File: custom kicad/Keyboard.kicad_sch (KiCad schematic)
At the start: 1 part, among them U1 nRF52840

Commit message: started custom pcb
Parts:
- removed U1: nRF52840, Package_DFN_QFN:Nordic_AQFN-73-1EP_7x7mm_P0.5mm, symbol MCU_Nordic:nRF52840
- added D1, D10, D100, D101, D102, D11, D12, D13, D14, D15, D16, D17, D18, D19, D2, D20, D21, D22, D23, D24, D25, D26, D27, D28, D29, D3, D30, D32, D33, D34, D35, D36, D39, D4, D40, D41, D42, D43, D44, D45, D46, D47, D48, D49, D5, D50, D51, D52, D53, D54, D55, D56, D57, D58, D59, D6, D60, D61, D62, D63, D65, D66, D67, D68, D7, D70, D71, D72, D73, D75, D76, D77, D78, D79, D8, D81, D83, D84, D85, D87, D89, D9, D91, D92, D94, D95, D96, D98, D99: D_Small, symbol Device:D_Small
- added J1: Conn_02x20_Top_Bottom, symbol Connector_Generic:Conn_02x20_Top_Bottom
- added MX1, MX10, MX100, MX101, MX102, MX11, MX12, MX13, MX14, MX15, MX16, MX17, MX18, MX19, MX2, MX20, MX21, MX22, MX23, MX24, MX25, MX26, MX27, MX28, MX29, MX3, MX30, MX32, MX33, MX34, MX35, MX36, MX39, MX4, MX40, MX41, MX42, MX43, MX44, MX45, MX46, MX47, MX48, MX49, MX5, MX50, MX51, MX52, MX53, MX54, MX55, MX56, MX57, MX58, MX59, MX6, MX60, MX61, MX62, MX63, MX65, MX66, MX67, MX68, MX7, MX70, MX71, MX72, MX73, MX75, MX76, MX77, MX78, MX79, MX8, MX81, MX83, MX84, MX85, MX87, MX89, MX9, MX91, MX92, MX94, MX95, MX96, MX98, MX99: MX_SW_HS, PCM_marbastlib-mx:SW_MX_HS_CPG151101S11_1u, symbol marbastlib-mx:MX_SW_HS_CPG151101S11
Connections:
- new net: D67.2 (A), MX67.2
- new net: D48.2 (A), MX48.2
- new net: D81.2 (A), MX81.2
- new net: D41.2 (A), MX41.2
- new net: D77.2 (A), MX77.2
- new net: D42.2 (A), MX42.2
- new net: D53.2 (A), MX53.2
- new net: D91.2 (A), MX91.2
- new net: D56.2 (A), MX56.2
- new net: D33.2 (A), MX33.2
- new net: D30.2 (A), MX30.2
- new net: D40.2 (A), MX40.2
- new net: D36.2 (A), MX36.2
- new net: D50.2 (A), MX50.2
- new net: D26.2 (A), MX26.2
- new net: D49.2 (A), MX49.2
- new net: D19.2 (A), MX19.2
- new net: D92.2 (A), MX92.2
- new net: D73.2 (A), MX73.2
- new net: D8.2 (A), MX8.2
- new net: D79.2 (A), MX79.2
- new net: D22.2 (A), MX22.2
- new net: D6.2 (A), MX6.2
- new net: D78.2 (A), MX78.2
- new net: D39.2 (A), MX39.2
- new net: D58.2 (A), MX58.2
- new net: D96.2 (A), MX96.2
- new net: D13.2 (A), MX13.2
- new net: D68.2 (A), MX68.2
- new net: D14.2 (A), MX14.2
- new net: D34.2 (A), MX34.2
- new net: D83.2 (A), MX83.2
- new net: D102.2 (A), MX102.2
- new net: D44.2 (A), MX44.2
- new net: D65.2 (A), MX65.2
- new net: D11.2 (A), MX11.2
- new net: D54.2 (A), MX54.2
- new net: D87.2 (A), MX87.2
- new net: D101.2 (A), MX101.2
- new net: D57.2 (A), MX57.2
- new net: D20.2 (A), MX20.2
- new net: D59.2 (A), MX59.2
- new net: D12.2 (A), MX12.2
- new net: D24.2 (A), MX24.2
- new net: D47.2 (A), MX47.2
- new net: D18.2 (A), MX18.2
- new net: D55.2 (A), MX55.2
- new net: D1.2 (A), MX1.2
- new net: D94.2 (A), MX94.2
- new net: D100.2 (A), MX100.2
- new net: D29.2 (A), MX29.2
- new net: D72.2 (A), MX72.2
- new net: D66.2 (A), MX66.2
- new net: D95.2 (A), MX95.2
- new net: D46.2 (A), MX46.2
- new net: D17.2 (A), MX17.2
- new net: D25.2 (A), MX25.2
- new net: D99.2 (A), MX99.2
- new net: D71.2 (A), MX71.2
- new net: D62.2 (A), MX62.2
- new net: D3.2 (A), MX3.2
- new net: D76.2 (A), MX76.2
- new net: D85.2 (A), MX85.2
- new net: D2.2 (A), MX2.2
- new net: D32.2 (A), MX32.2
- new net: D10.2 (A), MX10.2
- new net: D27.2 (A), MX27.2
- new net: D5.2 (A), MX5.2
- new net: D61.2 (A), MX61.2
- new net: D84.2 (A), MX84.2
- new net: D21.2 (A), MX21.2
- new net: D70.2 (A), MX70.2
- new net: D23.2 (A), MX23.2
- new net: D52.2 (A), MX52.2
- new net: D7.2 (A), MX7.2
- new net: D15.2 (A), MX15.2
- new net: D28.2 (A), MX28.2
- new net: D51.2 (A), MX51.2
- new net: D4.2 (A), MX4.2
- new net: D63.2 (A), MX63.2
- new net: D9.2 (A), MX9.2
- new net: D45.2 (A), MX45.2
- new net: D98.2 (A), MX98.2
- new net: D60.2 (A), MX60.2
- new net: D43.2 (A), MX43.2
- new net: D89.2 (A), MX89.2
- new net: D75.2 (A), MX75.2
- new net: D16.2 (A), MX16.2
- new net: D35.2 (A), MX35.2
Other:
- removed sheet MCU

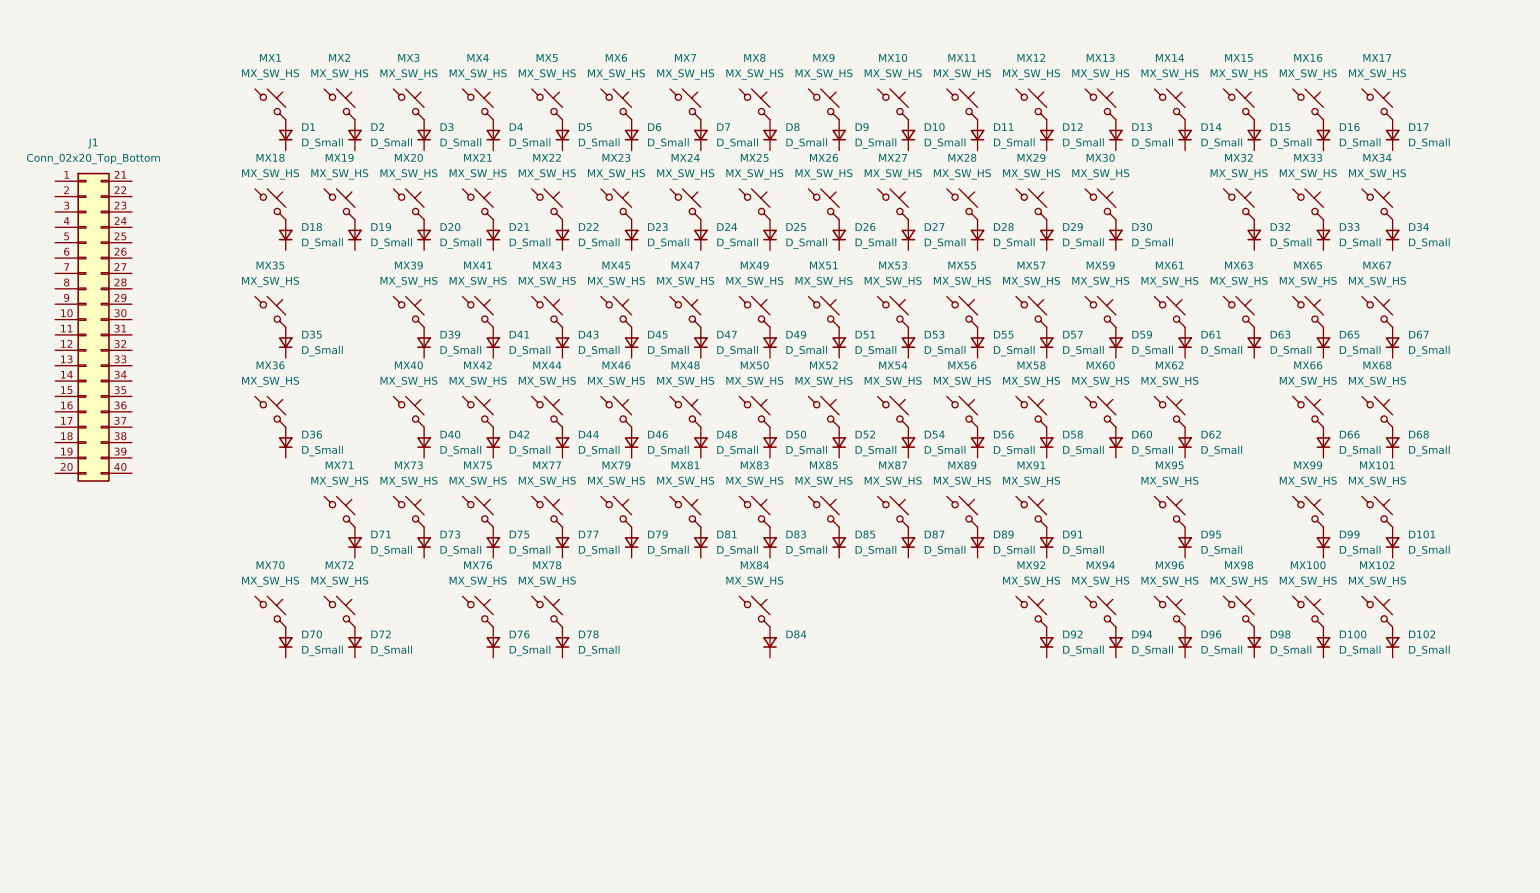
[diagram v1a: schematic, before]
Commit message: wired custom pcb, need blackpill footprint
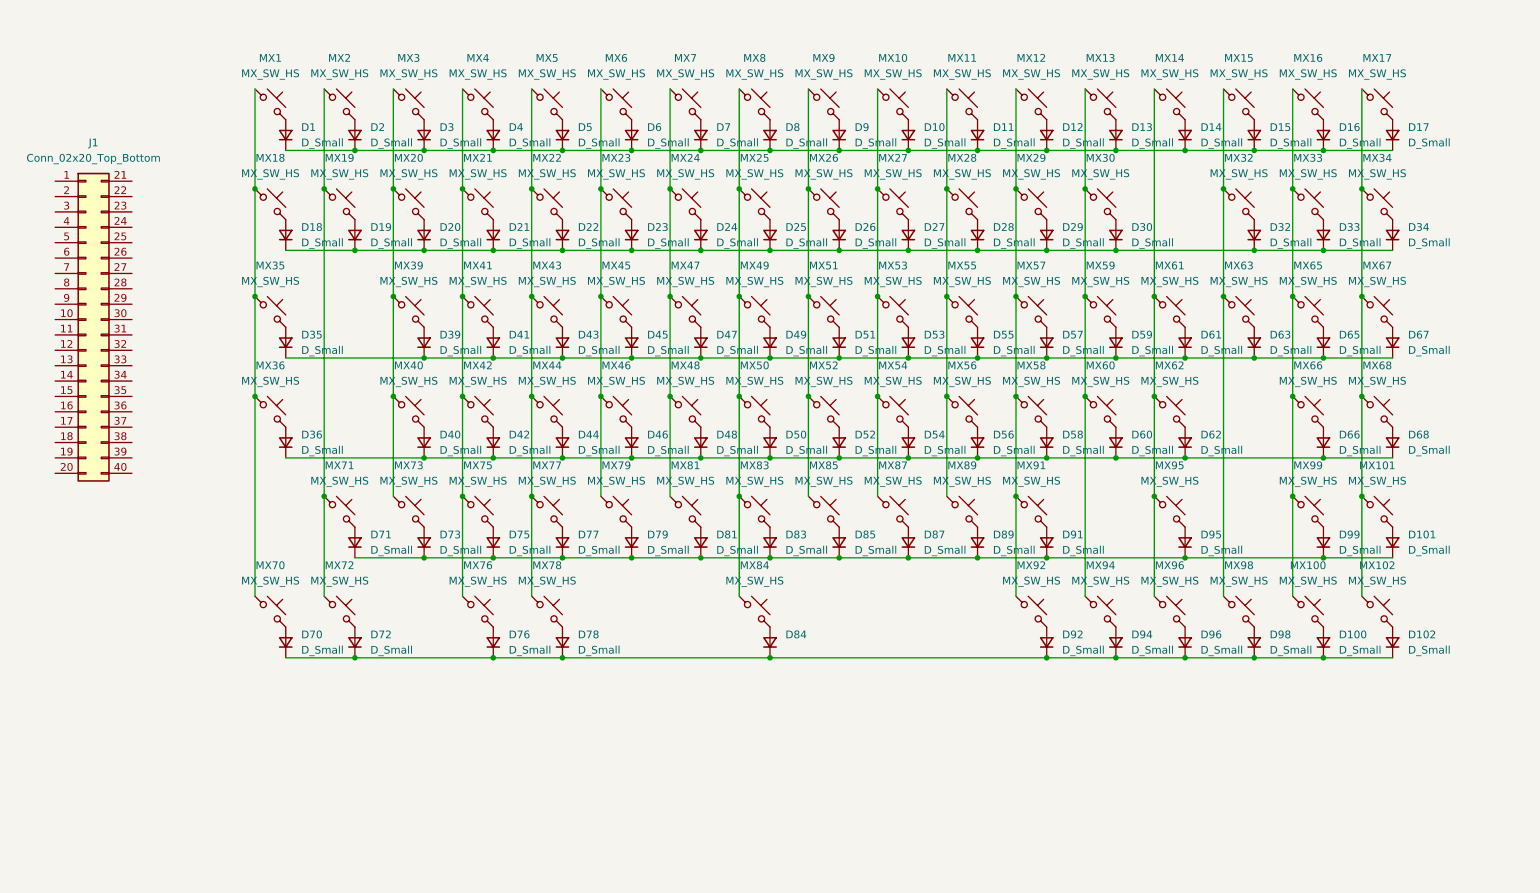
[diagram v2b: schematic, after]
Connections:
- net at D67.1 (K): now also D35.1 (K), D39.1 (K), D41.1 (K), D43.1 (K), D45.1 (K), D47.1 (K), D49.1 (K), D51.1 (K), D53.1 (K), D55.1 (K), D57.1 (K), D59.1 (K), D61.1 (K), D63.1 (K), D65.1 (K)
- net at D48.1 (K): now also D36.1 (K), D40.1 (K), D42.1 (K), D44.1 (K), D46.1 (K), D50.1 (K), D52.1 (K), D54.1 (K), D56.1 (K), D58.1 (K), D60.1 (K), D62.1 (K), D66.1 (K), D68.1 (K)
- net at D81.1 (K): now also D101.1 (K), D71.1 (K), D73.1 (K), D75.1 (K), D77.1 (K), D79.1 (K), D83.1 (K), D85.1 (K), D87.1 (K), D89.1 (K), D91.1 (K), D95.1 (K), D99.1 (K)
- net at MX41.1: now also MX21.1, MX4.1, MX42.1, MX75.1, MX76.1
- net at MX77.1: now also MX22.1, MX43.1, MX44.1, MX5.1, MX78.1
- net at MX91.1: now also MX12.1, MX29.1, MX57.1, MX58.1, MX92.1
- net at MX56.1: now also MX11.1, MX28.1, MX55.1, MX89.1
- net at MX33.1: now also MX100.1, MX16.1, MX65.1, MX66.1, MX99.1
- net at MX30.1: now also MX13.1, MX59.1, MX60.1, MX94.1
- net at MX36.1: now also MX1.1, MX18.1, MX35.1, MX70.1
- net at MX48.1: now also MX24.1, MX47.1, MX7.1, MX81.1
- net at MX67.1: now also MX101.1, MX102.1, MX17.1, MX34.1, MX68.1
- net at MX26.1: now also MX51.1, MX52.1, MX85.1, MX9.1
- net at MX19.1: now also MX2.1, MX71.1, MX72.1
- net at MX8.1: now also MX25.1, MX49.1, MX50.1, MX83.1, MX84.1
- net at MX79.1: now also MX23.1, MX45.1, MX46.1, MX6.1
- net at D78.1 (K): now also D100.1 (K), D102.1 (K), D70.1 (K), D72.1 (K), D76.1 (K), D84.1 (K), D92.1 (K), D94.1 (K), D96.1 (K), D98.1 (K)
- net at D14.1 (K): now also D1.1 (K), D10.1 (K), D11.1 (K), D12.1 (K), D13.1 (K), D15.1 (K), D16.1 (K), D17.1 (K), D2.1 (K), D3.1 (K), D4.1 (K), D5.1 (K), D6.1 (K), D7.1 (K), D8.1 (K), D9.1 (K)
- net at D34.1 (K): now also D18.1 (K), D19.1 (K), D20.1 (K), D21.1 (K), D22.1 (K), D23.1 (K), D24.1 (K), D25.1 (K), D26.1 (K), D27.1 (K), D28.1 (K), D29.1 (K), D30.1 (K), D32.1 (K), D33.1 (K)
- net at MX96.1: now also MX14.1, MX61.1, MX62.1, MX95.1
- net at MX53.1: now also MX10.1, MX27.1, MX54.1, MX87.1
- net at MX3.1: now also MX20.1, MX39.1, MX40.1, MX73.1
- net at MX32.1: now also MX15.1, MX63.1, MX98.1
